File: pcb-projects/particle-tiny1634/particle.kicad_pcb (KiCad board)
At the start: 2 copper layers, 43.2 x 43.7 mm, 32 parts, among them CON1 AVR-ISP-6, IC1 ATTINY1634-SU, P1 TXN, P2 RXN, P3 TXS, P4 RXS, P5 TRXCH

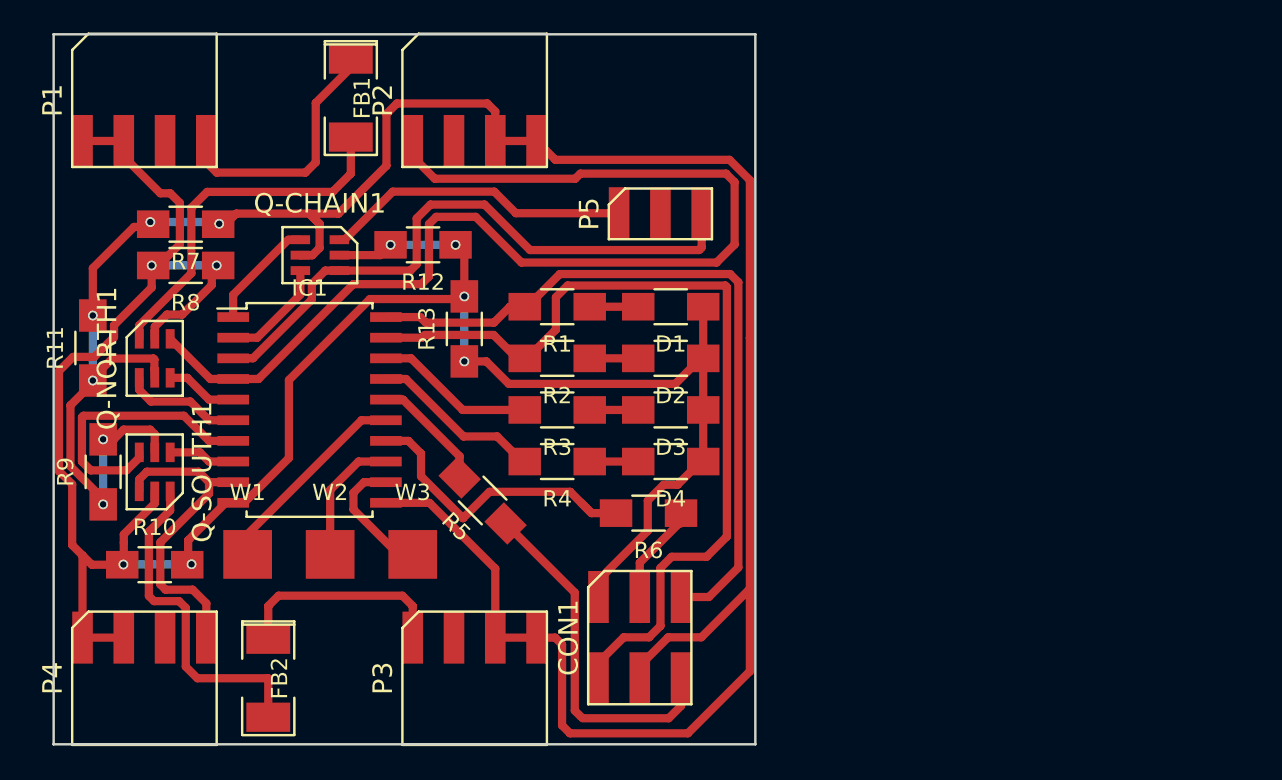
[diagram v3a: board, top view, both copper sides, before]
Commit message: re-routed smaller pcb, added several 3d packages, min. fix in schema
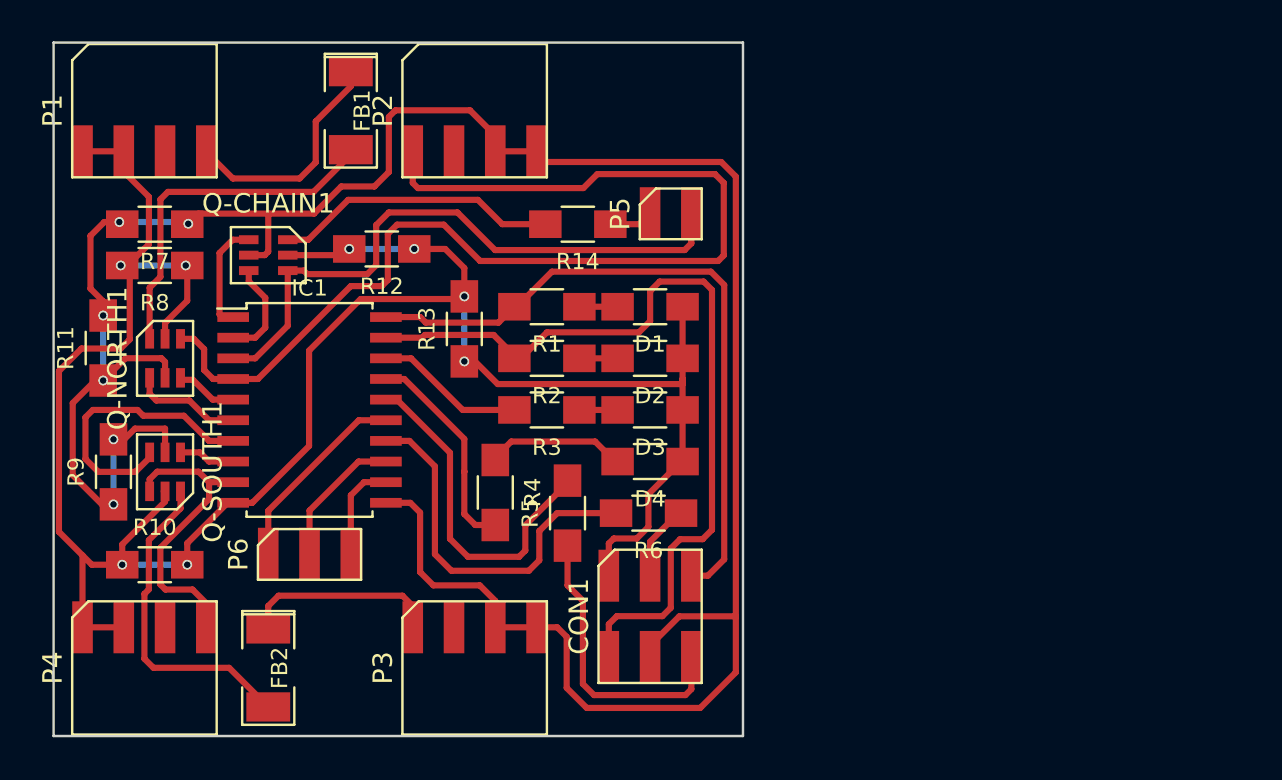
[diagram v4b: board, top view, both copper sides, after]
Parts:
- removed W1, W2, W3: TEST_1P, Measurement_Points:Measurement_Point_Square-SMD-Pad_Big
- added P6: TEST1-3, SMT_PIN_HEADER:CONN-1x3, F.Cu at (149.9, 116.8)
- added R14: 1k2, Resistors_SMD:R_1206_HandSoldering, F.Cu at (166.4, 96.5)
- P5: value TRXCH -> TRX-CH; footprint SMT_PIN_HEADER:CONN-1x3 -> SMT_PIN_HEADER:CONN-1x2
- moved R5 5.28 mm to (165.7, 114.3), turned to 90 degrees
- moved R4 4.26 mm to (161.3, 113.0), turned to 270 degrees
- moved Q-CHAIN1 3.18 mm to (147.3, 98.4)
- moved R12 2.55 mm to (154.3, 98.0)
- moved R7 1.91 mm to (140.3, 96.5)
- moved R8 1.91 mm to (140.3, 99.1)
- moved CON1 1.46 mm to (170.8, 120.7)
- moved D1 1.27 mm to (170.8, 101.6)
- moved D2 1.27 mm to (170.8, 104.8)
- moved D3 1.27 mm to (170.8, 108.0)
- moved D4 1.27 mm to (170.8, 111.1)
- moved FB1 0.77 mm to (152.4, 89.5)
- moved P4 0.64 mm to (139.7, 123.8)
- moved P5 0.64 mm to (172.1, 95.9)
- moved FB2 0.63 mm to (147.3, 123.8)
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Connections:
- P5 pad 2: (no net) -> /RX-CHAIN
- Q-CHAIN1 pad 6: /TX-CHAIN -> Net-(Q-CHAIN1-Pad6)
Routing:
- net Net-(Q-CHAIN1-Pad6): track 0.00 -> 17.5 mm
- net /TX-CHAIN: track 19.0 -> 2.72 mm
- net Net-(IC1-Pad16): track 7.96 -> 21.2 mm
- net Net-(D4-Pad2): track 2.99 -> 8.70 mm
- net Net-(IC1-Pad14): track 19.0 -> 23.8 mm
- net /SCK: track 21.9 -> 18.0 mm
- net /MOSI: track 45.1 -> 41.9 mm
- net /ERROR: track 10.6 -> 13.8 mm
- net /TP3: track 8.09 -> 6.09 mm
- net VCC: track 160.0 -> 158.1 mm
- net /MISO: track 54.2 -> 52.4 mm
- net GND: track 144.5 -> 142.9 mm
- net /TX-NORTH: track 15.8 -> 14.9 mm
- net /RST: track 5.65 -> 4.73 mm
- net Net-(FB2-Pad2): track 20.9 -> 20.1 mm
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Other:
- board size 43.2 x 43.7 mm -> 42.4 x 42.7 mm
- net class Default: trace_width 0.508 -> 0.381

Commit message: added all 3d models, pcb cosmetics
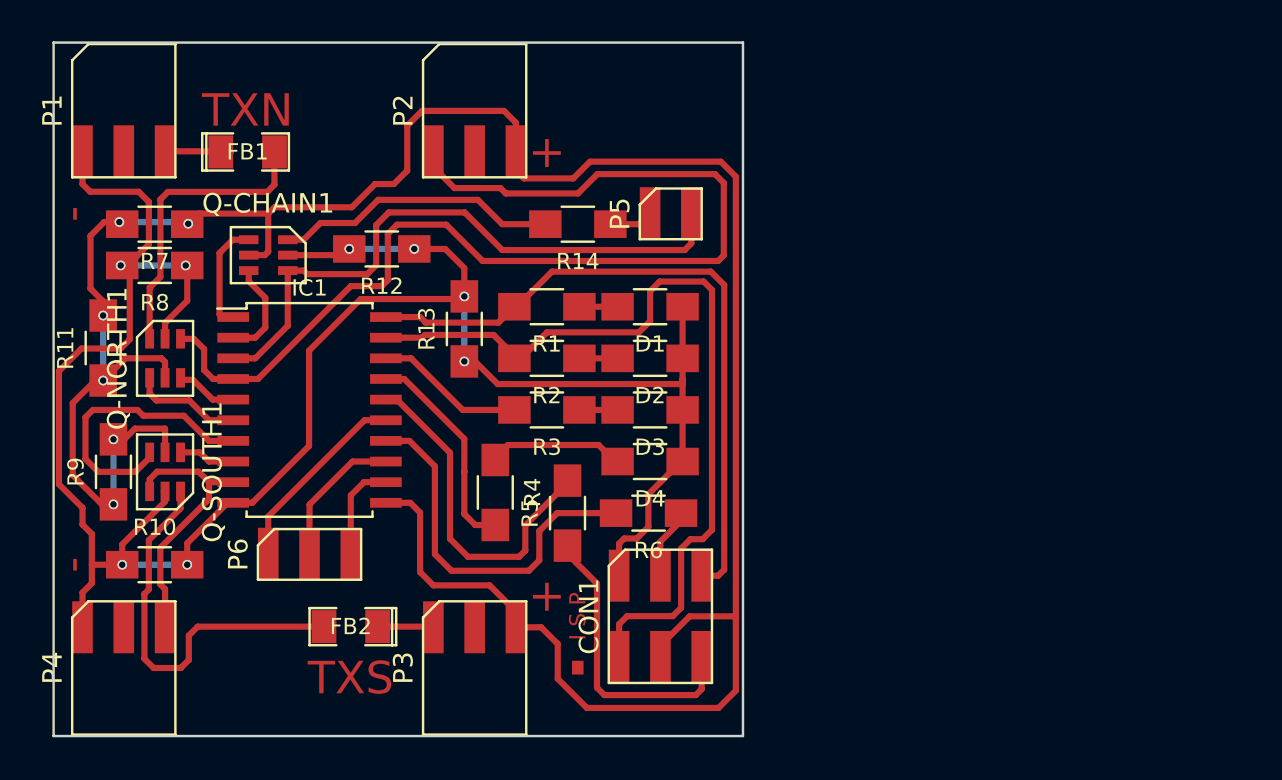
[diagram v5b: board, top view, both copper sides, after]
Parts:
- FB1: value TX-SMA-N -> TXN-SMA; footprint SMD_Packages:SMD-2010_Pol -> SMD_Packages:SMD-1206_Pol
- FB2: value TX-SMA-S -> TXS-SMA; footprint SMD_Packages:SMD-2010_Pol -> SMD_Packages:SMD-1206_Pol
- P1, P2: footprint SMT_PIN_HEADER:CONN-8_1-4 -> SMT_PIN_HEADER:CONN-6_1-3
- P3, P4: footprint SMT_PIN_HEADER:CONN-8_5-8 -> SMT_PIN_HEADER:CONN-6_4-6
- moved FB1 6.84 mm to (146.1, 92.1), turned to 0 degrees
- moved FB2 5.68 mm to (152.4, 121.3), turned to 180 degrees
- moved P1 1.27 mm to (138.4, 89.5)
- moved P4 1.27 mm to (138.4, 123.8)
- moved CON1 0.63 mm to (171.4, 120.7)
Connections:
- P1 pad 2: GND -> (no net)
- P1 pad 3: (no net) -> /TX-NORTH
- P3 pad 5: VCC -> (no net)
- P3 pad 6: VCC -> /TX-SOUTH
- P4 pad 5: /RX-SOUTH -> (no net)
- P4 pad 6: (no net) -> GND
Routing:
- net /TX-NORTH: track 14.9 -> 3.50 mm
- net /TX-SOUTH: track 12.8 -> 3.45 mm
- net Net-(FB2-Pad2): track 20.1 -> 24.4 mm
- net GND: track 142.9 -> 139.0 mm
- net Net-(FB1-Pad2): track 22.0 -> 18.3 mm
- net /RX-SOUTH: track 20.6 -> 18.0 mm
- net /RX-NORTH: track 69.0 -> 67.4 mm
- net /MISO: track 52.4 -> 51.8 mm
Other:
- board text added: "+"
- board text added: "-"
- board text added: "."
- board text added: "I S P"
- board text added: "TXN"
- board text added: "TXS"

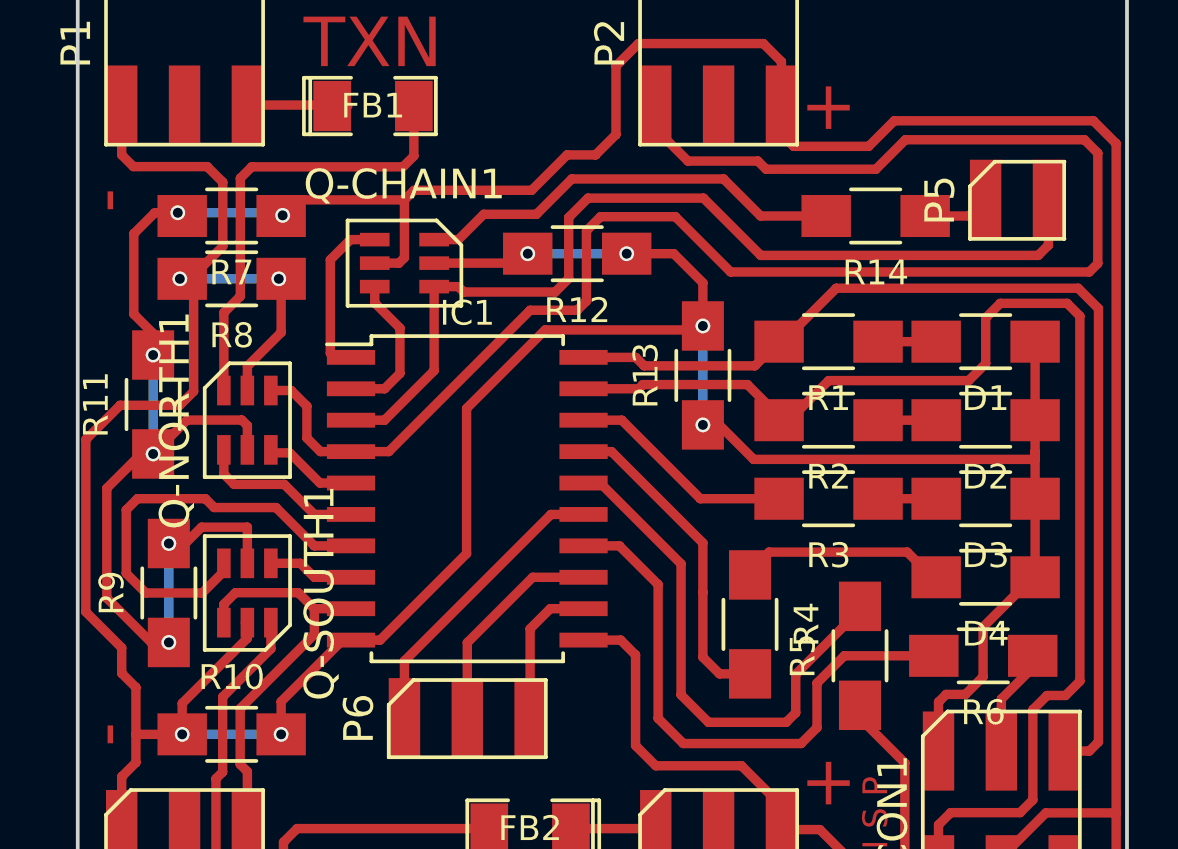
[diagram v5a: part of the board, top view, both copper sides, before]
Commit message: increased clearance from 0.2mm to 0.33mm
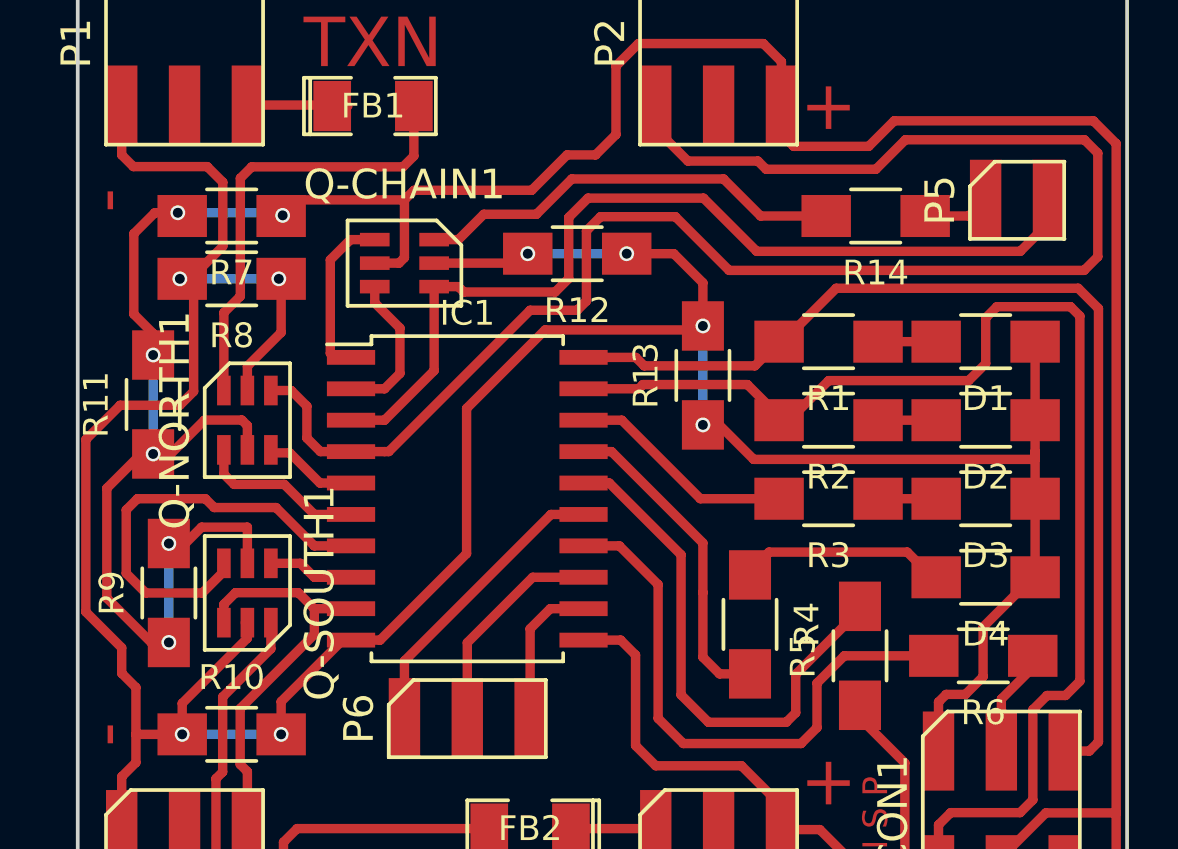
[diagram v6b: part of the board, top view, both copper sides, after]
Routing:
- net /RX-CHAIN: track 38.5 -> 37.9 mm
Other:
- net class Default: clearance 0.2 -> 0.38
- rule trace_clearance: 0.2 -> 0.38

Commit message: added usb connector module/3d
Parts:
- R10, R11, R12, R13, R5, R6, R7, R8, R9: value 0 -> 0R
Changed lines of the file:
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@@
-(kicad_pcb (version 4) (host pcbnew 4.0.1-3.201512221402+6198~38~ubuntu15.04.1-stable)
+(kicad_pcb (version 4) (host pcbnew 4.0.1-3.201512221401+6198~38~ubuntu15.10.1-stable)
   (general
-    (links 65)
-    (no_connects 0)
-    (area 132.79 85.159999 176.867857 128.200001)
+    (links 68)
+    (no_connects 3)
+    (area 134.036999 85.268233 176.606712 128.091737)
     (thickness 1.6)
     (drawings 12)
@@
     (add_net "Net-(IC1-Pad14)")
     (add_net "Net-(IC1-Pad16)")
+    (add_net "Net-(P7-Pad1)")
     (add_net "Net-(Q-CHAIN1-Pad6)")
     (add_net VCC)
@@
       (effects (font (size 1 1) (thickness 0.15)))
     )
-    (fp_text value 0 (at 0 2.3 180) (layer F.Fab)
+    (fp_text value 0R (at 0 2.3 180) (layer F.Fab)
       (effects (font (size 1 1) (thickness 0.15)))
     )
@@
       (effects (font (size 1 1) (thickness 0.15)))
     )
-    (fp_text value 0 (at 0 2.3 90) (layer F.Fab)
+    (fp_text value 0R (at 0 2.3 90) (layer F.Fab)
       (effects (font (size 1 1) (thickness 0.15)))
     )
@@
       (effects (font (size 1 1) (thickness 0.15)))
     )
-    (fp_text value 0 (at 0 2.3 180) (layer F.Fab)
+    (fp_text value 0R (at 0 2.3 180) (layer F.Fab)
       (effects (font (size 1 1) (thickness 0.15)))
     )
@@
       (effects (font (size 1 1) (thickness 0.15)))
     )
-    (fp_text value 0 (at 0 2.3 180) (layer F.Fab)
+    (fp_text value 0R (at 0 2.3 180) (layer F.Fab)
       (effects (font (size 1 1) (thickness 0.15)))
     )
@@
       (effects (font (size 1 1) (thickness 0.15)))
     )
-    (fp_text value 0 (at 0 2.3 180) (layer F.Fab)
+    (fp_text value 0R (at 0 2.3 180) (layer F.Fab)
       (effects (font (size 1 1) (thickness 0.15)))
     )
@@
       (effects (font (size 1 1) (thickness 0.15)))
     )
-    (fp_text value 0 (at 0 2.3 90) (layer F.Fab)
+    (fp_text value 0R (at 0 2.3 90) (layer F.Fab)
       (effects (font (size 1 1) (thickness 0.15)))
     )
@@
       (effects (font (size 1 1) (thickness 0.15)))
     )
-    (fp_text value 0 (at 0 2.3) (layer F.Fab)
+    (fp_text value 0R (at 0 2.3) (layer F.Fab)
       (effects (font (size 1 1) (thickness 0.15)))
     )
@@
       (effects (font (size 1 1) (thickness 0.15)))
     )
-    (fp_text value 0 (at 0 2.3 90) (layer F.Fab)
+    (fp_text value 0R (at 0 2.3 90) (layer F.Fab)
       (effects (font (size 1 1) (thickness 0.15)))
     )
@@
       (effects (font (size 1 1) (thickness 0.15)))
     )
-    (fp_text value 0 (at 0 2.3 90) (layer F.Fab)
-      (effects (font (size 1 1) (thickness 0.15)))
-    )
+    (fp_text value 0R (at 0 2.3 90) (layer F.Fab)
+      (effects (font (size 1 1) (thickness 0.15)))
+    )

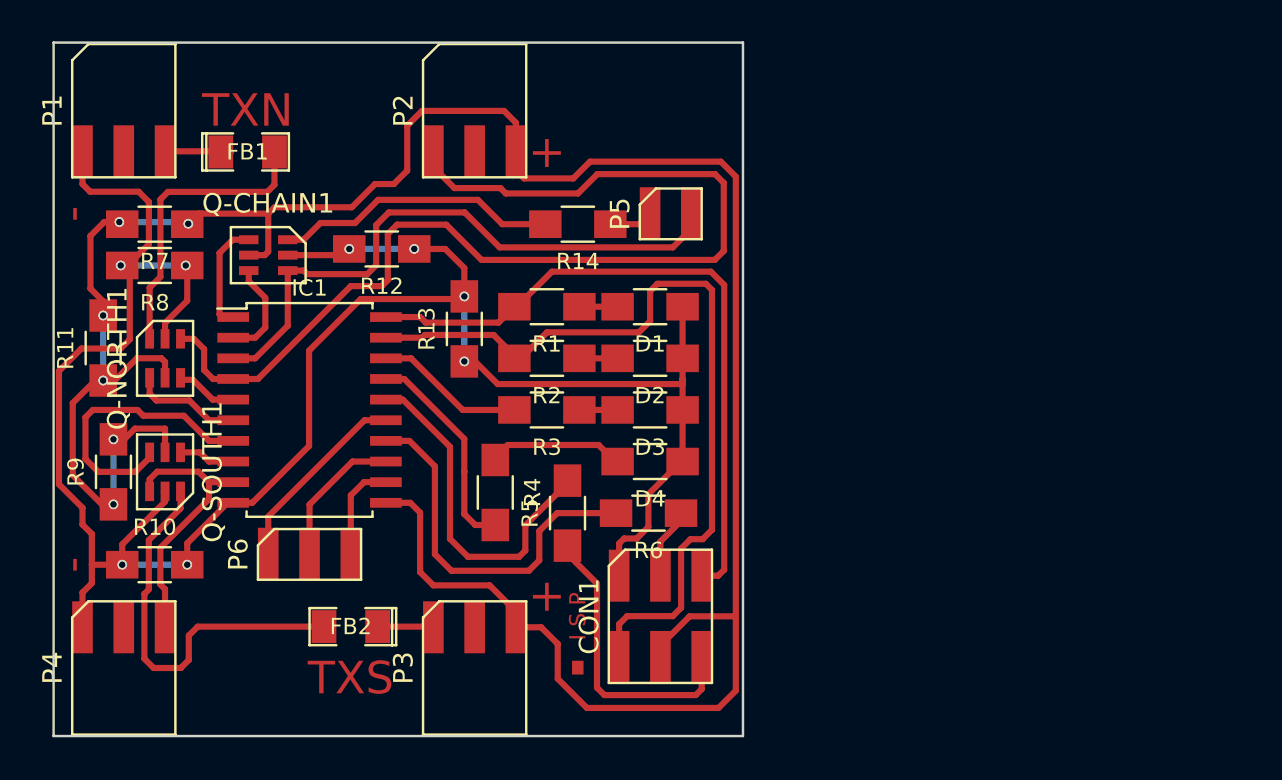
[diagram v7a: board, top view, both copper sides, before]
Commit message: minor edge cut alignment, added particle array
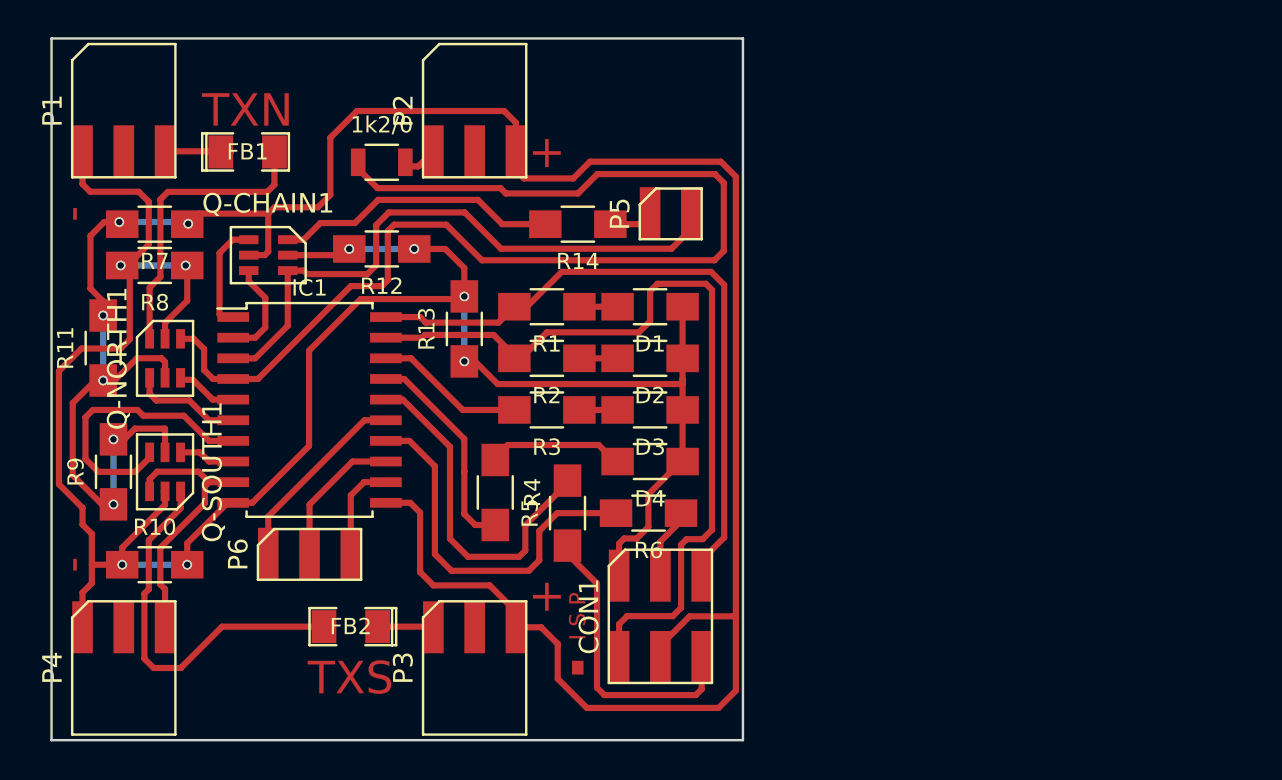
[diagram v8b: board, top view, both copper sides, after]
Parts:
- added 1k2/0: 1k2, Resistors_SMD:R_1206, F.Cu at (154.3, 92.7)
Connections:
- P2 pad 1: /RX-NORTH -> Net-(1k2/0-Pad2)
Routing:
- net /RX-NORTH: track 67.2 -> 71.5 mm
- net Net-(1k2/0-Pad2): track 0.00 -> 1.98 mm
- net Net-(FB2-Pad2): track 24.4 -> 23.6 mm
- net /MOSI: track 41.7 -> 41.1 mm
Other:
- board size 42.4 x 42.7 mm -> 42.5 x 43.2 mm
- net class Default: clearance 0.38 -> 0.33
- rule trace_clearance: 0.38 -> 0.33
- rule trace_min: 0.2 -> 0.007874
- rule via_min_size: 0.4 -> 0.015748
